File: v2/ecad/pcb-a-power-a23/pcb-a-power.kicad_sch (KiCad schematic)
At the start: 603 parts, among them Q1 2N7002: panel controller high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, Q10 CSD18510Q5B 40 V N-FET, Q11 CSD18510Q5B 40 V N-FET, Q12 CSD18510Q5B 40 V N-FET, Q13 CSD18510Q5B 40 V N-FET, Q14 CSD18510Q5B 40 V N-FET, Q15 CSD18510Q5B 40 V N-FET, Q16 CSD18510Q5B 40 V N-FET, Q17 CSD19532Q5B 100 V N-FET (4.6 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, Q18 CSD19532Q5B 100 V N-FET (4.6 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, Q19 CSD19532Q5B 100 V N-FET (4.6 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, Q2 CSD19532Q5B 100 V N-FET (4.6 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, Q20 CSD19532Q5B 100 V N-FET (4.6 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, Q21 CSD18510Q5B 40 V N-FET, Q22 CSD18510Q5B 40 V N-FET, Q23 CSD18510Q5B 40 V N-FET, Q24 CSD18510Q5B 40 V N-FET, Q25 CSD18510Q5B 40 V N-FET, Q26 CSD18510Q5B 40 V N-FET, Q27 CSD18510Q5B 40 V N-FET (VBUS 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, Q28 CSD19532Q5B 100 V N-FET (4.6 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, Q29 CSD19532Q5B 100 V N-FET (4.6 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, Q3 CSD19532Q5B 100 V N-FET (4.6 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, Q30 CSD19532Q5B 100 V N-FET (4.6 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, Q31 CSD19532Q5B 100 V N-FET (4.6 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, Q32 CSD19532Q5B 100 V N-FET (4.6 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, Q33 CSD19532Q5B 100 V N-FET (4.6 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, Q34 CSD19532Q5B 100 V N-FET (4.6 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, Q35 CSD19532Q5B 100 V N-FET (4.6 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, Q36 2N7002: FE_RUN high = latch s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, Q37 2N7002: FE_RUN high = bleed o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, Q38 CSD19532Q5B 100 V N-FET (the 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, Q4 CSD19532Q5B 100 V N-FET (4.6 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, Q5 CSD19532Q5B 100 V N-FET (4.6 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, Q6 2N7002: CHG_INHIBIT high = IL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, Q7 CSD18510Q5B 40 V N-FET, Q8 CSD18510Q5B 40 V N-FET, Q9 CSD18510Q5B 40 V N-FET, U1 LTC2954ITS8-1 push-button on/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, U10 INA226 rail monitor +5V_S3, U11 INA226 rail monitor +5V_DEV, U12 TPS62933DRLR 3 A buck, 3.3 V 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, U13 LM5176PWPR buck-boost control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, U14 INA226 PA rail monitor (0x46), U15 LM5176PWPR buck-boost control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, U16 LM5176PWPR buck-boost control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, U17 INA226 PoE rail monitor (0x47), U18 TPS25740ARGER USB-C PD source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, U19 LM5176PWPR buck-boost control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, U2 LM5176PWPR buck-boost control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, U21 TPS259631DDAR eFuse VBAT -> V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, U22 TPS259631DDAR eFuse VBAT -> V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, U23 TPS259631DDAR eFuse +5V_DEV -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, U26 SN74LVC08APWR quad AND: the o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, U27 PCA9555PW (0x21): enables and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, U28 PCA9555PW (0x24): power-good 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, U29 USBLC6-2SC6, U3 BQ25731RSNR 1 to 5 cell buck-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, U30 SN74LVC1G00DBVR NAND: OUTLET_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, U31 TPD2E2U06QDBZRQ1 low-capacita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, U32 TPS259631DDAR eFuse +5V_DEV -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, U33 TPS62933DRLR 3 A buck, 12.0 V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, U34 TPS37A010122DSKR 65 V OV/UV s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, U35 SN74AUP1G08DBVR AND: PA_TXOK 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, U36 SN74AUP1G08DBVR AND: PA_EN = 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, U37 SN74AUP1G08DBVR AND: HF_TXOK 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, U38 SN74AUP1G08DBVR AND: HF_EN = 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, U39 TPS259631DDAR eFuse +3V3 -> +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, U4 AP64500SP-13 5 A buck, 5.1 V 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, U40 SN74LVC2G07DBVR dual open-dra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, U5 LM5176PWPR buck-boost control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, U6 AP64500SP-13 5 A buck, 5.1 V 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, U7 LM5176PWPR buck-boost control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, U8 INA226 rail monitor +5V_S1, U9 INA226 rail monitor +5V_S2

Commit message: fix(pcb-d,pcb-e): declare the supplies PWR-001 refused, sense the tracker's current on its bottom leg, and carry VIN_RAW across the dock on power pins with board A's half [MESHSAT-1357]
Boards D and E, stream w3de (27 September 2026, from main 0598e8e5), integrated in fnd/r8int5 on main 68a83858 with
board A's half of EQ-16 on board A's w3a generator. The session's engineering choices are recorded as SC-55 to SC-57
with reason and reversal, never as the owner's. Prototype: no board is built.

PWR-001 (EQ-19): each supply the rule refused on D and E is declared with the kind its maker's sheet gives. The parts'
own regulator outputs, charge pumps and bootstraps are nodes (D: PCM2912A outputs, SAU_3V3, AMP_CPP, AMP_CPN,
AMP_HPVSS; E: TRK_LDO33, E6_DVDD, E6_BST); SGP_VDD, another part's filtered branch, is a rail. PWR-001 read
INCONCLUSIVE on D (RLY_K) and E (FAN1_SW, FAN2_SW) with no failure in the stream's scratch, the three awaiting the
flyback diodes' sheets (S-76).

S-47: the LT8705A's sense resistor R5 moves to the bottom switches' leg as the maker draws it (8705af Figure 1): the
new node TRK_CS joins Q4's and Q5's sources above R5, L1 joins TRK_SW1 to TRK_SW2, MODE is tied to LDO33, GATEVCC and
VIN get their own bypass capacitors (C63, C64). TRK_CS is a switching net in board E's pre-lay group and in
pcb_sensitive.yaml's switch list, as board A's LM5176 CS nodes are.

EQ-16 / R8E-N01: at board E's 14.10 A the four Preci-Dip 813 VIN_RAW contacts ran at 3.53 A each against 3.5 A.
VIN_RAW now crosses the dock on four Mill-Max 9 A power pins with four return pins, as CELL+ does, and the four 813
contacts become ground. Board E's half (J_BLK, P_VR, P_VN) and board A's (J_VR1-4, J_VN1-4, J_DOCK, VIN_RAW declared
at 14.10 A) land together, with the IF-AE-DOCK contract and check_contracts.py's dock checks: PASS 99 of 99 on this
tree's netlists (verdicts in scratch).

Parity: stream w3de regenerated D and E on the KiCad box with main's chain; D's netlist is identical in e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
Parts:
- removed C113, C153, C222, C28, C40: 100n, Capacitor_SMD:C_0603_1608Metric, symbol Device:C
- removed C134, C141, C27: 1n, Capacitor_SMD:C_0603_1608Metric, symbol Device:C
- removed C148, C149: 470p, Capacitor_SMD:C_0603_1608Metric, symbol Device:C
- removed C158, C26: 10n, Capacitor_SMD:C_0603_1608Metric, symbol Device:C
- removed C23, C24: 22u 25V 1210, Capacitor_SMD:C_1210_3225Metric, symbol Device:C
- removed C34, C79: 100n 25V, Capacitor_SMD:C_0603_1608Metric, symbol Device:C
- removed C86, C94: 220n, Capacitor_SMD:C_0603_1608Metric, symbol Device:C
- removed C87: 1.5n, Capacitor_SMD:C_0603_1608Metric, symbol Device:C
- removed C88: 47n, Capacitor_SMD:C_0603_1608Metric, symbol Device:C
- removed D15, D16: BAT46W-7-F Schottky 100V (bootstrap), Diode_SMD:D_SOD-123, symbol Device:D_Schottky
- removed D22: BZT52C12-7-F zener, the restart guard's pull-up c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, Diode_SMD:D_SOD-123, symbol Device:D_Zener
- removed J_BM11: SMP-MAX slide-on receptacle R222M00720 (underside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, meshsat:Radiall_SMPMAX_R222M00720, symbol Connector:Conn_Coaxial
- removed L10: 15uH XAL1010-153ME (Isat 15.5 A), Inductor_SMD:L_Coilcraft_XAL1010-XXX, symbol Device:L
- removed Q19: CSD19532Q5B 100 V N-FET (4.6 mOhm at VGS 6 V, Pow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, Package_SO:PowerPAK_SO-8_Single, symbol meshsat_ic:Q19
- removed R10: 15k, Resistor_SMD:R_0603_1608Metric, symbol Device:R
- removed R123, R178, R30: 100k, Resistor_SMD:R_0603_1608Metric, symbol Device:R
- removed R130: 2.2k, Resistor_SMD:R_0603_1608Metric, symbol Device:R
- removed R137: 14.0k 1% (R_FBL1: 15 V when CTL1 is low too), Resistor_SMD:R_0603_1608Metric, symbol Device:R
- removed R15, R51: 10k 1%, Resistor_SMD:R_0603_1608Metric, symbol Device:R
- removed R180: 100R 1% (CS filter, Kelvin from the shunt's top), Resistor_SMD:R_0603_1608Metric, symbol Device:R
- removed R23, R25: 10k, Resistor_SMD:R_0603_1608Metric, symbol Device:R
- removed R27: 40.2k 1%, Resistor_SMD:R_0603_1608Metric, symbol Device:R
- removed R32, R40: 53.6k 1%, Resistor_SMD:R_0603_1608Metric, symbol Device:R
- removed R80: 3.3k, Resistor_SMD:R_0603_1608Metric, symbol Device:R
- removed U22: TPS259631DDAR eFuse VBAT -> VHEAT_IN (909R 1% (IL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, Package_SO:SOIC-8-1EP_3.9x4.9mm_P1.27mm_EP2.29x3mm, symbol meshsat_ic:U22
- added C112: 3.3n, Capacitor_SMD:C_0603_1608Metric, symbol Device:C
- added C119, C21, C22, C74, C82: 10u 50V X7R 1210, Capacitor_SMD:C_1210_3225Metric, symbol Device:C
- added C138: 1n, Capacitor_SMD:C_0603_1608Metric, symbol Device:C
- added C144, C16, C46, C90: 100n 25V, Capacitor_SMD:C_0603_1608Metric, symbol Device:C
- added C161, C37: 22u 25V 1210, Capacitor_SMD:C_1210_3225Metric, symbol Device:C
- added C174: 470u 25V Panasonic EEHZK1E471P hybrid polymer (10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, Capacitor_SMD:CP_Elec_10x10, symbol Device:C_Polarized
- added C18: 3.3u, Capacitor_SMD:C_0805_2012Metric, symbol Device:C
- added C193, C197, C219, C221: 100n, Capacitor_SMD:C_0603_1608Metric, symbol Device:C
- added C41: 10u 25V 1210, Capacitor_SMD:C_1210_3225Metric, symbol Device:C
- added C60: 4.7u, Capacitor_SMD:C_0805_2012Metric, symbol Device:C
- added C83: 10u 100V X7R 1210, Capacitor_SMD:C_1210_3225Metric, symbol Device:C
- added D12, D14, D17, D18, D8: BAT46W-7-F Schottky 100V (bootstrap), Diode_SMD:D_SOD-123, symbol Device:D_Schottky
- added J_VN1, J_VN2, J_VN3, J_VN4: 9 A spring pin, VIN_RAW return (Mill-Max 0858 cla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, meshsat:Mill-Max_0858_power_pin, symbol Connector:Conn_01x01_Pin
- added J_VR1, J_VR2, J_VR3, J_VR4: 9 A spring pin, VIN_RAW (Mill-Max 0858 class, doc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, meshsat:Mill-Max_0858_power_pin, symbol Connector:Conn_01x01_Pin
- added L1: 10uH XAL1010-103ME (Isat 17.5 A), Inductor_SMD:L_Coilcraft_XAL1010-XXX, symbol Device:L
- added L2: 3.3uH XAL6030-332ME (Isat 12.2 A), Inductor_SMD:L_Coilcraft_XAL6060-XXX, symbol Device:L
- added L3: 4.7uH XAL6060-472ME (Isat 11 A), Inductor_SMD:L_Coilcraft_XAL6060-XXX, symbol Device:L
- added L6: 6.8uH XAL1010-682ME (Isat 21.8 A), Inductor_SMD:L_Coilcraft_XAL1010-XXX, symbol Device:L
- added Q22: CSD18510Q5B 40 V N-FET, Package_SO:PowerPAK_SO-8_Single, symbol meshsat_ic:Q22
- added Q36: 2N7002: FE_RUN high = latch sense held at 0 V (1 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, Package_TO_SOT_SMD:SOT-23, symbol Transistor_FET:2N7002
- added Q38: CSD19532Q5B 100 V N-FET (the VBUS20 bleed switch), Package_SO:PowerPAK_SO-8_Single, symbol meshsat_ic:Q38
- added R139: 43R 1W 2512 (DSCG), Resistor_SMD:R_2512_6332Metric, symbol Device:R
- added R171: 100k, Resistor_SMD:R_0603_1608Metric, symbol Device:R
- added R18: 10R, Resistor_SMD:R_0603_1608Metric, symbol Device:R
- added R19: 16.5k 1%, Resistor_SMD:R_0603_1608Metric, symbol Device:R
- added R96: 143k 1%, Resistor_SMD:R_0603_1608Metric, symbol Device:R
- added TP17: SDA, TestPoint:TestPoint_Pad_D1.5mm, symbol Connector:TestPoint
- added U17: INA226 PoE rail monitor (0x47), Package_SO:VSSOP-10_3x3mm_P0.5mm, symbol meshsat_ic:U17
- added U27: PCA9555PW (0x21): enables and status, Package_SO:TSSOP-24_4.4x7.8mm_P0.65mm, symbol Interface_Expansion:PCA9555PW
- C113: renamed from R171; value 100k -> 100n; footprint Resistor_SMD:R_0603_1608Metric -> Capacitor_SMD:C_0603_1608Metric; symbol Device:R -> Device:C; LCSC (none) -> C14663
- C117: renamed from C90; value 100n 25V -> 10u 50V X7R 1210; footprint Capacitor_SMD:C_0603_1608Metric -> Capacitor_SMD:C_1210_3225Metric
- C118: renamed from D17; value BAT46W-7-F Schottky 100V (bootstrap) -> 10u 50V X7R 1210; footprint Diode_SMD:D_SOD-123 -> Capacitor_SMD:C_1210_3225Metric; symbol Device:D_Schottky -> Device:C; LCSC C83152 -> (none)
- C134: renamed from C137; value 100n 25V -> 1n; LCSC (none) -> C1588
- C137: renamed from C193; value 100n -> 100n 25V
- C141: renamed from C146; LCSC (none) -> C1588
- C146: renamed from C144; value 100n 25V -> 1n
- C148: renamed from D12; value BAT46W-7-F Schottky 100V (bootstrap) -> 470p; footprint Diode_SMD:D_SOD-123 -> Capacitor_SMD:C_0603_1608Metric; symbol Device:D_Schottky -> Device:C; LCSC C83152 -> C27694
- C149: renamed from D14; value BAT46W-7-F Schottky 100V (bootstrap) -> 470p; footprint Diode_SMD:D_SOD-123 -> Capacitor_SMD:C_0603_1608Metric; symbol Device:D_Schottky -> Device:C; LCSC C83152 -> C27694
- C153: renamed from U27; value PCA9555PW (0x21): enables and status -> 100n; footprint Package_SO:TSSOP-24_4.4x7.8mm_P0.65mm -> Capacitor_SMD:C_0603_1608Metric; symbol Interface_Expansion:PCA9555PW -> Device:C; LCSC C2864778 -> (none)
- C158: renamed from C161; value 22u 25V 1210 -> 10n; footprint Capacitor_SMD:C_1210_3225Metric -> Capacitor_SMD:C_0603_1608Metric
- C17: renamed from L2; value 3.3uH XAL6030-332ME (Isat 12.2 A) -> 100n 25V; footprint Inductor_SMD:L_Coilcraft_XAL6060-XXX -> Capacitor_SMD:C_0603_1608Metric; symbol Device:L -> Device:C
- C222: renamed from Q22; value CSD18510Q5B 40 V N-FET -> 100n; footprint Package_SO:PowerPAK_SO-8_Single -> Capacitor_SMD:C_0603_1608Metric; symbol meshsat_ic:Q22 -> Device:C; LCSC (none) -> C14663
- C23: renamed from C21; value 10u 50V X7R 1210 -> 22u 25V 1210
- C24: renamed from C22; value 10u 50V X7R 1210 -> 22u 25V 1210
- C26: renamed from R18; value 10R -> 10n; footprint Resistor_SMD:R_0603_1608Metric -> Capacitor_SMD:C_0603_1608Metric; symbol Device:R -> Device:C
- C27: renamed from R19; value 16.5k 1% -> 1n; footprint Resistor_SMD:R_0603_1608Metric -> Capacitor_SMD:C_0603_1608Metric; symbol Device:R -> Device:C
- C28: renamed from C112; value 3.3n -> 100n
- C34: renamed from C37; value 22u 25V 1210 -> 100n 25V; footprint Capacitor_SMD:C_1210_3225Metric -> Capacitor_SMD:C_0603_1608Metric; LCSC C2918511 -> (none)
- C40: renamed from C41; value 10u 25V 1210 -> 100n; footprint Capacitor_SMD:C_1210_3225Metric -> Capacitor_SMD:C_0603_1608Metric
- C79: renamed from C197; value 100n -> 100n 25V
- C86: renamed from C119; value 10u 50V X7R 1210 -> 220n; footprint Capacitor_SMD:C_1210_3225Metric -> Capacitor_SMD:C_0603_1608Metric; LCSC (none) -> C160828
- C87: renamed from C174; value 470u 25V Panasonic EEHZK1E471P hybrid polymer (10.2 mm) -> 1.5n; footprint Capacitor_SMD:CP_Elec_10x10 -> Capacitor_SMD:C_0603_1608Metric; symbol Device:C_Polarized -> Device:C; LCSC C242138 -> C37788
- C88: renamed from C117; value 10u 50V X7R 1210 -> 47n; footprint Capacitor_SMD:C_1210_3225Metric -> Capacitor_SMD:C_0603_1608Metric
- C94: renamed from R139; value 43R 1W 2512 (DSCG) -> 220n; footprint Resistor_SMD:R_2512_6332Metric -> Capacitor_SMD:C_0603_1608Metric; symbol Device:R -> Device:C
- D15: renamed from C221; value 100n -> BAT46W-7-F Schottky 100V (bootstrap); footprint Capacitor_SMD:C_0603_1608Metric -> Diode_SMD:D_SOD-123; symbol Device:C -> Device:D_Schottky; LCSC C14663 -> C83152
- D16: renamed from C82; value 10u 50V X7R 1210 -> BAT46W-7-F Schottky 100V (bootstrap); footprint Capacitor_SMD:C_1210_3225Metric -> Diode_SMD:D_SOD-123; symbol Device:C -> Device:D_Schottky; LCSC (none) -> C83152
- D22: renamed from Q38; value CSD19532Q5B 100 V N-FET (the VBUS20 bleed switch) -> BZT52C12-7-F zener, the restart guard's pull-up clamp; footprint Package_SO:PowerPAK_SO-8_Single -> Diode_SMD:D_SOD-123; symbol meshsat_ic:Q38 -> Device:D_Zener; LCSC C473333 -> C124196
- D6: renamed from C219; value 100n -> BAT46W-7-F Schottky 100V (bootstrap); footprint Capacitor_SMD:C_0603_1608Metric -> Diode_SMD:D_SOD-123; symbol Device:C -> Device:D_Schottky; LCSC C14663 -> C83152
- J_BM11: renamed from TP17; value SDA -> SMP-MAX slide-on receptacle R222M00720 (underside), LORA to the dock plug; footprint TestPoint:TestPoint_Pad_D1.5mm -> meshsat:Radiall_SMPMAX_R222M00720; symbol Connector:TestPoint -> Connector:Conn_Coaxial; now in the parts list
- J_DOCK: value spring pins to the dock block (2x6, Preci-Dip 813-S1-012-10-016101, underside): 1-4 VIN_RAW (9 to 36 V from E6), 5-7 GN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 -> spring pins to the dock block (2x6, Preci-Dip 813-S1-012-10-016101, underside): 1-7 GND, 8 SHORE_INHIBIT, 9-10 USB of E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
- L10: renamed from C83; value 10u 100V X7R 1210 -> 15uH XAL1010-153ME (Isat 15.5 A); footprint Capacitor_SMD:C_1210_3225Metric -> Inductor_SMD:L_Coilcraft_XAL1010-XXX; symbol Device:C -> Device:L; LCSC (none) -> C2802562
- Q19: renamed from U17; value INA226 PoE rail monitor (0x47) -> CSD19532Q5B 100 V N-FET (4.6 mOhm at VGS 6 V, PowerPAK SO-8 / SON-8 5x6); footprint Package_SO:VSSOP-10_3x3mm_P0.5mm -> Package_SO:PowerPAK_SO-8_Single; symbol meshsat_ic:U17 -> meshsat_ic:Q19; LCSC C49851 -> C473333
- R10: renamed from L1; value 10uH XAL1010-103ME (Isat 17.5 A) -> 15k; footprint Inductor_SMD:L_Coilcraft_XAL1010-XXX -> Resistor_SMD:R_0603_1608Metric; symbol Device:L -> Device:R; LCSC C6358489 -> C22809
- R123: renamed from C74; value 10u 50V X7R 1210 -> 100k; footprint Capacitor_SMD:C_1210_3225Metric -> Resistor_SMD:R_0603_1608Metric; symbol Device:C -> Device:R
- R130: renamed from C138; value 1n -> 2.2k; footprint Capacitor_SMD:C_0603_1608Metric -> Resistor_SMD:R_0603_1608Metric; symbol Device:C -> Device:R; LCSC (none) -> C4190
- R137: renamed from D18; value BAT46W-7-F Schottky 100V (bootstrap) -> 14.0k 1% (R_FBL1: 15 V when CTL1 is low too); footprint Diode_SMD:D_SOD-123 -> Resistor_SMD:R_0603_1608Metric; symbol Device:D_Schottky -> Device:R; LCSC C83152 -> (none)
- R15: renamed from Q36; value 2N7002: FE_RUN high = latch sense held at 0 V (1 G, 2 S, 3 D) -> 10k 1%; footprint Package_TO_SOT_SMD:SOT-23 -> Resistor_SMD:R_0603_1608Metric; symbol Transistor_FET:2N7002 -> Device:R; LCSC C8545 -> C25804
- R178: renamed from L6; value 6.8uH XAL1010-682ME (Isat 21.8 A) -> 100k; footprint Inductor_SMD:L_Coilcraft_XAL1010-XXX -> Resistor_SMD:R_0603_1608Metric; symbol Device:L -> Device:R
- R180: renamed from C46; value 100n 25V -> 100R 1% (CS filter, Kelvin from the shunt's top); footprint Capacitor_SMD:C_0603_1608Metric -> Resistor_SMD:R_0603_1608Metric; symbol Device:C -> Device:R
- R181: renamed from D8; value BAT46W-7-F Schottky 100V (bootstrap) -> 100R 1% (CSG filter, Kelvin from the shunt's ground pad); footprint Diode_SMD:D_SOD-123 -> Resistor_SMD:R_0603_1608Metric; symbol Device:D_Schottky -> Device:R; LCSC C83152 -> (none)
- R23: renamed from C17; value 100n 25V -> 10k; footprint Capacitor_SMD:C_0603_1608Metric -> Resistor_SMD:R_0603_1608Metric; symbol Device:C -> Device:R
- R25: renamed from C18; value 3.3u -> 10k; footprint Capacitor_SMD:C_0805_2012Metric -> Resistor_SMD:R_0603_1608Metric; symbol Device:C -> Device:R
- R27: renamed from C16; value 100n 25V -> 40.2k 1%; footprint Capacitor_SMD:C_0603_1608Metric -> Resistor_SMD:R_0603_1608Metric; symbol Device:C -> Device:R
- R30: renamed from L3; value 4.7uH XAL6060-472ME (Isat 11 A) -> 100k; footprint Inductor_SMD:L_Coilcraft_XAL6060-XXX -> Resistor_SMD:R_0603_1608Metric; symbol Device:L -> Device:R
- R32: renamed from D6; value BAT46W-7-F Schottky 100V (bootstrap) -> 53.6k 1%; footprint Diode_SMD:D_SOD-123 -> Resistor_SMD:R_0603_1608Metric; symbol Device:D_Schottky -> Device:R; LCSC C83152 -> (none)
- R40: renamed from R181; value 100R 1% (CSG filter, Kelvin from the shunt's ground pad) -> 53.6k 1%
- R51: renamed from C60; value 4.7u -> 10k 1%; footprint Capacitor_SMD:C_0805_2012Metric -> Resistor_SMD:R_0603_1608Metric; symbol Device:C -> Device:R
- R80: renamed from C118; value 10u 50V X7R 1210 -> 3.3k; footprint Capacitor_SMD:C_1210_3225Metric -> Resistor_SMD:R_0603_1608Metric; symbol Device:C -> Device:R; LCSC (none) -> C22978
- U22: renamed from R96; value 143k 1% -> TPS259631DDAR eFuse VBAT -> VHEAT_IN (909R 1% (ILM: 1.0 A)); footprint Resistor_SMD:R_0603_1608Metric -> Package_SO:SOIC-8-1EP_3.9x4.9mm_P1.27mm_EP2.29x3mm; symbol Device:R -> meshsat_ic:U22; LCSC C22877 -> C2155778
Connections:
- net +3V3: now also C153.1, R123.2, R178.2, R23.2, R171.2, U17.1 (+3V3), U17.6 (+3V3), U27.21 (A0), U27.24 (VDD); no longer C113.2, C153.21 (A0), C153.24 (VDD), Q19.1 (+3V3), Q19.6 (+3V3)
- net +54V_POE: now also C83.1, U17.9 (+54V_POE); no longer L10.1, Q19.9 (+54V_POE)
- net +5V_DEV: now also R40.1
- net +5V_S2: now also R32.1, C37.1; no longer C34.1
- net CHG_ILIM: now also R19.2; no longer C27.2
- net CHG_INHIBIT: now also U27.4 (IO0_0); no longer C153.4 (IO0_0)
- net CHRG_OK: now also U27.13 (IO1_0); no longer C153.13 (IO1_0)
- net CH_BTST1: now also C16.1; no longer R27.1
- net CH_BTST2: now also C17.1; no longer R23.1
- net CH_CELL: now also R27.1
- net CH_COMP1: now also R25.1
- net CH_COMP1C: now also C26.1, R25.2
- net CH_COMP2: now also C27.1
- net CH_SW1: now also C16.2, L2.1; no longer C17.1, R27.2
- net CH_SW2: now also L2.2; no longer R23.2
- net CH_VDDA: now also R18.2; no longer C26.2
- net D8_EN: now also U27.7 (IO0_3); no longer C153.7 (IO0_3)
- net D8_FLT: now also U27.17 (IO1_4); no longer C153.17 (IO1_4)
- net DEV_EN: now also U27.11 (IO0_7); no longer C153.11 (IO0_7)
- net DOCK_SPARE: now also U27.18 (IO1_5); no longer C153.18 (IO1_5)
- net EXP_INT: now also U27.1 (~{INT}); no longer C153.1 (~{INT})
- net FE_BLEED: now also Q38.5 (FE_BLEED); no longer D22.5 (FE_BLEED)
- net FE_BLEED_G: now also Q38.4 (FE_BLEED_G); no longer D22.4 (FE_BLEED_G)
- net FE_COMP: now also R10.1
- net FE_COMPC: now also R10.2
- net FE_LATCH: now also Q36.3 (D); no longer R15.3 (D)
- net FE_PGOOD: now also U27.20 (IO1_7); no longer C153.20 (IO1_7)
- net FE_RUN: now also Q36.1 (G); no longer R15.1 (G)
- net FE_SW1: now also L1.1; no longer R10.1
- net FE_SW2: now also L1.2; no longer R10.2
- net FE_UVS: now also R15.1
- net FE_VZ: now also D22.1 (K)
- net GND: now also C113.2, C117.2, C118.2, C134.2, C141.2, C148.2, C149.2, C222.2, C26.2, C27.2, C94.2, J_BM11.2 (Ext)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; no longer C137.2, C153.12 (VSS), C153.3 (A2), C28.2, C34.2, C40.2, C79.2, D15.2, D16.2, D22.1 (GND), D22.3 (GND), D6.2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
- net HEAT_EN: now also U22.3 (HEAT_EN), U27.6 (IO0_2); no longer C153.6 (IO0_2)
- net HEAT_FLT: now also U22.6 (HEAT_FLT), U27.16 (IO1_3); no longer C153.16 (IO1_3)
- net HF_BOOT2: now also D14.1 (K); no longer C149.1 (K)
- net HF_PGOOD: now also R123.1
- net HF_SLOPE: now also C149.1
- net HF_SW_EN: now also U27.10 (IO0_6); no longer C153.10 (IO0_6)
- net HF_VCC: now also D14.2 (A); no longer C149.2 (A)
- net HT_SS: now also C158.1
- net INA_ALERT: now also U17.3 (INA_ALERT), U27.19 (IO1_6); no longer C153.19 (IO1_6), Q19.3 (INA_ALERT)
- net MON_EN: now also U27.5 (IO0_1); no longer C153.5 (IO0_1)
- net MON_FLT: now also U27.15 (IO1_2); no longer C153.15 (IO1_2)
- net PA_BOOT2: now also D12.1 (K); no longer C148.1 (K)
- net PA_FB: now also R51.1
- net PA_SLOPE: now also C148.1
- net PA_SW_EN: now also U27.9 (IO0_5); no longer C153.9 (IO0_5)
- net PA_VCC: now also C60.1, D12.2 (A); no longer C148.2 (A), R51.1
- net PD_BOOT1: now also C90.1, D17.1 (K); no longer C117.1, C118.1 (K)
- net PD_BOOT2: now also D18.1 (K); no longer R137.1 (K)
- net PD_COMP: now also C87.1, R80.1
- net PD_COMPC: now also C86.1, R80.2
- net PD_CS: now also Q22.1 (PD_CS), Q22.2 (PD_CS), Q22.3 (PD_CS); no longer C222.1 (PD_CS), C222.2 (PD_CS), C222.3 (PD_CS)
- net PD_CTL1: now also R137.2
- net PD_DSCG: now also R139.1; no longer C94.1
- net PD_DVDD: now also C94.1
- net PD_FB: now also R137.1
- net PD_LDRV1: now also Q22.4 (PD_LDRV1); no longer C222.4 (PD_LDRV1)
- net PD_SS: now also C88.1
- net PD_SW1: now also C90.2, Q22.5 (PD_SW1); no longer C117.2, C222.5 (PD_SW1)
- net PD_VBUS: now also R139.2; no longer C94.2
- net PD_VCC: now also D17.2 (A), D18.2 (A); no longer C118.2 (A), R137.2 (A)
- net PD_VPWR: now also C117.1, C118.1, C119.1, C174.1; no longer C86.1, C87.1, C88.1, R80.1
- net POE_BOOT1: now also C79.1, D15.1 (K)
- net POE_BOOT2: now also D16.1 (K)
- net POE_CS: now also Q19.1 (POE_CS), Q19.2 (POE_CS), Q19.3 (POE_CS)
- net POE_LDRV2: now also Q19.4 (POE_LDRV2)
- net POE_OUT: now also U17.10 (POE_OUT); no longer Q19.10 (POE_OUT)
- net POE_SW1: now also C79.2, L10.1
- net POE_SW2: now also L10.2, Q19.5 (POE_SW2)
- net POE_SW_EN: now also U27.8 (IO0_4); no longer C153.8 (IO0_4)
- net POE_VCC: now also D15.2 (A), D16.2 (A)
- net PROCHOT: now also R23.1, U27.14 (IO1_1); no longer C153.14 (IO1_1)
- net REGN: now also C18.1, R18.1, R19.1; no longer C26.1, C27.1, R25.1
- net RF_LORA: now also J_BM11.1 (In)
- net S1_BOOT: now also C28.1
- net S1_COMPC: now also C112.1; no longer C28.1
- net S1_OUT: now also L3.2; no longer R30.2
- net S1_SW: now also C28.2, L3.1; no longer R30.1
- net S2_BOOT1: now also C34.1
- net S2_BOOT2: now also C137.1, D6.1 (K); no longer C134.1, R32.1 (K)
- net S2_COMP: now also C134.1, R130.1
- net S2_COMPC: now also C113.1, R130.2
- net S2_CSF: now also C138.1; no longer R130.1
- net S2_CSGF: now also C138.2; no longer R130.2
- net S2_FB: now also R32.2
- net S2_PGOOD: now also R171.1; no longer C113.1
- net S2_SW1: now also C34.2
- net S2_SW2: now also C137.2; no longer C134.2
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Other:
- note added: "CHARGER BQ25731 | SLOT RAIL S1"
- note added: "CHARGER BQ25731: 4S FROM THE 20 V BUS, SYSTEM ON VSYS (VBAT), PACK BEYOND RSR, I2C 0x6B (continued)"
- note added: "DEVICE RAIL | 3.3 V LOGIC"
- note added: "DEVICE RAIL: LM5176 5.1 V (7.2 A MINIMUM LIMIT) + INA226 0x45 (continued)"
- note added: "HF RAIL"
- note added: "PA RAIL"
- note added: "PACK NODE OVER THE DOCK BLOCK (32.56) | MAIN POWER CONTROL LTC2954"
- note added: "SLOT RAIL S2"
- note added: "SLOT RAIL S3 | DEVICE RAIL"
- note added: "p1,15"
- note added: "p1,7,13"
- note added: "p1,7,15"
- note added: "p10,16"
- note added: "p11,12,16"
- note added: "p11,15"
- note added: "p11,15,16"
- note added: "p11,16"
- note added: "p12,15,16"
- note added: "p13,15"
- note added: "p15,16"
- note added: "p16"
- note added: "p2,16"
- note added: "p3,4,5,7,.."
- note added: "p3,4,6,7,.."
- note added: "p3,5,6,7,.."
- note added: "p4,15"
- note added: "p4,16"
- note added: "p4,5,6,7,.."
- note added: "p4,5,7,8,.."
- note added: "p5,6,7,8,.."
- note added: "p7,13,15"
- note added: "p8,13"
- note added: "p8,16"
- note added: "p9,16"
- note added: "page 1 of 16 MeshSat field kit V2, CERN-OHL-S-2.0 PROTOTYPE, nothing built 2026-09-27"
- note added: "page 10 of 16 MeshSat field kit V2, CERN-OHL-S-2.0 PROTOTYPE, nothing built 2026-09-27"
- note added: "page 11 of 16 MeshSat field kit V2, CERN-OHL-S-2.0 PROTOTYPE, nothing built 2026-09-27"
- note added: "page 12 of 16 MeshSat field kit V2, CERN-OHL-S-2.0 PROTOTYPE, nothing built 2026-09-27"
- note added: "page 13 of 16 MeshSat field kit V2, CERN-OHL-S-2.0 PROTOTYPE, nothing built 2026-09-27"
- note added: "page 14 of 16 MeshSat field kit V2, CERN-OHL-S-2.0 PROTOTYPE, nothing built 2026-09-27"
- note added: "page 15 of 16 MeshSat field kit V2, CERN-OHL-S-2.0 PROTOTYPE, nothing built 2026-09-27"
- note added: "page 16 of 16 MeshSat field kit V2, CERN-OHL-S-2.0 PROTOTYPE, nothing built 2026-09-27"
- note added: "page 2 of 16 MeshSat field kit V2, CERN-OHL-S-2.0 PROTOTYPE, nothing built 2026-09-27"
- note added: "page 3 of 16 MeshSat field kit V2, CERN-OHL-S-2.0 PROTOTYPE, nothing built 2026-09-27"
- note added: "page 4 of 16 MeshSat field kit V2, CERN-OHL-S-2.0 PROTOTYPE, nothing built 2026-09-27"
- note added: "page 5 of 16 MeshSat field kit V2, CERN-OHL-S-2.0 PROTOTYPE, nothing built 2026-09-27"
- note added: "page 6 of 16 MeshSat field kit V2, CERN-OHL-S-2.0 PROTOTYPE, nothing built 2026-09-27"
- note added: "page 7 of 16 MeshSat field kit V2, CERN-OHL-S-2.0 PROTOTYPE, nothing built 2026-09-27"
- note added: "page 8 of 16 MeshSat field kit V2, CERN-OHL-S-2.0 PROTOTYPE, nothing built 2026-09-27"
- note added: "page 9 of 16 MeshSat field kit V2, CERN-OHL-S-2.0 PROTOTYPE, nothing built 2026-09-27"
- note removed: "3.3 V LOGIC | PA RAIL"
- note removed: "DEVICE RAIL"
- note removed: "PA RAIL | HF RAIL"
- note removed: "PA RAIL: LM5176 13.8 V 6 A, EMCON GATED, INA226 0x46 (continued)"
- note removed: "PACK NODE OVER THE DOCK BLOCK (32.56) | MAIN POWER CONTROL LTC2954 | FRONT END"
- note removed: "SLOT RAIL S1 | SLOT RAIL S2"
- note removed: "SLOT RAIL S2 | SLOT RAIL S3"
- note removed: "SLOT RAIL S2: LM5176 5.1 V (7.2 A MINIMUM LIMIT) + INA226 0x41 (continued)"
- note removed: "p1,13"
- note removed: "p1,7,12"
- note removed: "p1,7,14"
- note removed: "p10,11,15"
- note removed: "p10,14"
- note removed: "p10,14,15"
- note removed: "p11,12"
- note removed: "p11,13"
- note removed: "p11,14,15"
- note removed: "p2,14"
- note removed: "p3,14"
- note removed: "p3,15"
- note removed: "p3,4,5,8,.."
- note removed: "p3,4,6,8,.."
- note removed: "p3,5,6,8,.."
- note removed: "p4,5,6,8,.."
- note removed: "p4,6,8,9,.."
- note removed: "p5,6,8,9,.."
- note removed: "p7,12"
- note removed: "p7,12,14"
- note removed: "p7,13"
- note removed: "p7,14,15"
- note removed: "p7,8,14"
- note removed: "p7,8,15"
- note removed: "p8,14,15"
- note removed: "p9,14"
- note removed: "page 1 of 15 MeshSat field kit V2, CERN-OHL-S-2.0 PROTOTYPE, nothing built 2026-09-27"
- note removed: "page 10 of 15 MeshSat field kit V2, CERN-OHL-S-2.0 PROTOTYPE, nothing built 2026-09-27"
- note removed: "page 11 of 15 MeshSat field kit V2, CERN-OHL-S-2.0 PROTOTYPE, nothing built 2026-09-27"
- note removed: "page 12 of 15 MeshSat field kit V2, CERN-OHL-S-2.0 PROTOTYPE, nothing built 2026-09-27"
- note removed: "page 13 of 15 MeshSat field kit V2, CERN-OHL-S-2.0 PROTOTYPE, nothing built 2026-09-27"
- note removed: "page 14 of 15 MeshSat field kit V2, CERN-OHL-S-2.0 PROTOTYPE, nothing built 2026-09-27"
- note removed: "page 15 of 15 MeshSat field kit V2, CERN-OHL-S-2.0 PROTOTYPE, nothing built 2026-09-27"
- note removed: "page 2 of 15 MeshSat field kit V2, CERN-OHL-S-2.0 PROTOTYPE, nothing built 2026-09-27"
- note removed: "page 3 of 15 MeshSat field kit V2, CERN-OHL-S-2.0 PROTOTYPE, nothing built 2026-09-27"
- note removed: "page 4 of 15 MeshSat field kit V2, CERN-OHL-S-2.0 PROTOTYPE, nothing built 2026-09-27"
- note removed: "page 5 of 15 MeshSat field kit V2, CERN-OHL-S-2.0 PROTOTYPE, nothing built 2026-09-27"
- note removed: "page 6 of 15 MeshSat field kit V2, CERN-OHL-S-2.0 PROTOTYPE, nothing built 2026-09-27"
- note removed: "page 7 of 15 MeshSat field kit V2, CERN-OHL-S-2.0 PROTOTYPE, nothing built 2026-09-27"
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
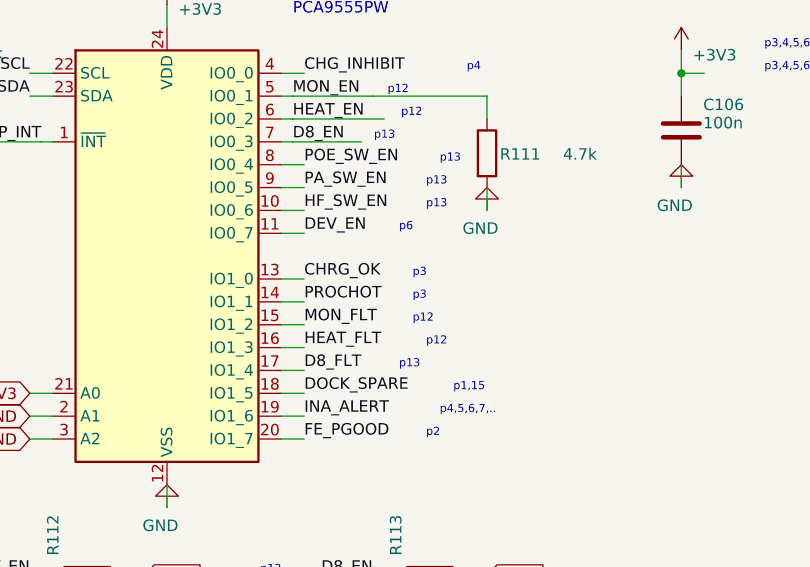
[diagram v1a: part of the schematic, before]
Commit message: feat(boards-a-e): the hot stop line HOT-R1 drawn on boards A and E, and board E's fan flyback sheet filed so PWR-001 reads PASS there [MESHSAT-1357]
Stream w4ae, from main 91894cd7, integrated with its drafts by r8int6 on main 6ec37197 after the w4r, w4b and w4c commits. Prototype design: nothing is built, ordered or measured.

HOT-R1 (S-57, SC-50, REQ-077). Board E: the sensor controller's GPIO19 (U10 pin 30) drives HOT_R1_G, the gate of Q11 (2N7002, the C8545 part of Q8 to Q10). Q11's open drain pulls BLK_SPARE (J_BLK pin 12, TP7) low, and R58 (100 k) holds the gate off while the controller is unpowered, in reset or booting. Board A: R216 (10 k 0603, as R110) pulls DOCK_SPARE (J_DOCK pin 12, U27 pin 18 P1.5, TP21) up to +3V3. No new part number and no new contact. The line is declared a safety line on both boards (A listens, safe high; E is the source), and the net names are kept.

The H2 path, read hop by hop on the committed netlists by v2/docs/records/w4ae/hot_r1_trace.py (on main's netlists it stops at U10 pin 30): an edge on U27 P1.5 raises EXP_INT (J_AB1 pin 13, board B, J_PANEL pin 6) at the panel controller's GPIO24. The panel controller reads U27 on the kit bus and, on a held low, drives PI_KILL (GPIO19, J_PANEL pin 25, board B, J_AB1 pin 10) into Q1. Q1 takes the LTC2954's KILL low, which drops RAIL_EN. No compute-module part is on the path: U27 runs on board A's +3V3, the panel controller on +5V_DEV, the sensor controller on CELL_F. The path is firmware in two controllers; S-58 stays open.

Board E's half of S-76 (SC-65). D7 and D8 carry their order code C51897884 (JLCPCB: SS14, Zhengxin, SMB). The maker's sheet is filed at v2/vendor/zhengxin/zhengxin-ss12-ss120-c51897884.pdf. FAN1_SW and FAN2_SW are declared nodes at 17.35 V (CELL_F's 16.8 V plus 0.55 V at 2.0 A).

Regenerated on the KiCad box with main's chain (PHASE A65 and E42P). Main's generators reproduce main's files and the new generators reproduce their own. The independent netlist comparison f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
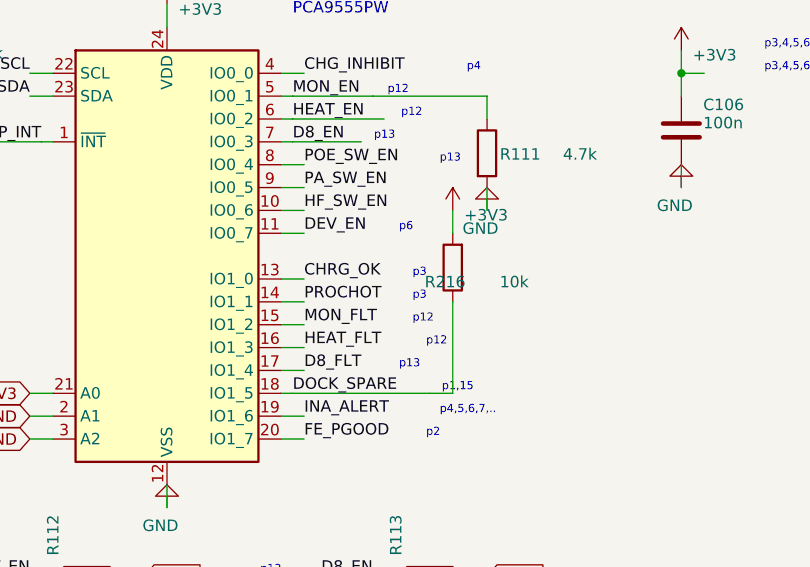
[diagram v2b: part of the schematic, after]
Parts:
- removed C123, C124, C125, C126, C127, C128, C129, C130, C131: 1n, Capacitor_SMD:C_0603_1608Metric, symbol Device:C
- added R152, R154, R156, R158: 100R 1% (CS filter, Kelvin from the shunt's top), Resistor_SMD:R_0603_1608Metric, symbol Device:R
- added R160, R162, R164, R166, R168: 100R 1% (ISNS+ filter, Kelvin from the shunt's ou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, Resistor_SMD:R_0603_1608Metric, symbol Device:R
- added R216: 10k, Resistor_SMD:R_0603_1608Metric, symbol Device:R
- C121: renamed from R148; value 10R -> 10n; footprint Resistor_SMD:R_0603_1608Metric -> Capacitor_SMD:C_0603_1608Metric; symbol Device:R -> Device:C
- C122: renamed from R152; value 100R 1% (CS filter, Kelvin from the shunt's top) -> 100n; footprint Resistor_SMD:R_0603_1608Metric -> Capacitor_SMD:C_0603_1608Metric; symbol Device:R -> Device:C
- C123: renamed from R160; value 100R 1% (ISNS+ filter, Kelvin from the shunt's output pad) -> 1n; footprint Resistor_SMD:R_0603_1608Metric -> Capacitor_SMD:C_0603_1608Metric; symbol Device:R -> Device:C
- C124: renamed from R162; value 100R 1% (ISNS+ filter, Kelvin from the shunt's output pad) -> 1n; footprint Resistor_SMD:R_0603_1608Metric -> Capacitor_SMD:C_0603_1608Metric; symbol Device:R -> Device:C
- C125: renamed from R164; value 100R 1% (ISNS+ filter, Kelvin from the shunt's output pad) -> 1n; footprint Resistor_SMD:R_0603_1608Metric -> Capacitor_SMD:C_0603_1608Metric; symbol Device:R -> Device:C
- C126: renamed from R166; value 100R 1% (ISNS+ filter, Kelvin from the shunt's output pad) -> 1n; footprint Resistor_SMD:R_0603_1608Metric -> Capacitor_SMD:C_0603_1608Metric; symbol Device:R -> Device:C
- C127: renamed from R168; value 100R 1% (ISNS+ filter, Kelvin from the shunt's output pad) -> 1n; footprint Resistor_SMD:R_0603_1608Metric -> Capacitor_SMD:C_0603_1608Metric; symbol Device:R -> Device:C
- C128: renamed from R146; value 10R -> 1n; footprint Resistor_SMD:R_0603_1608Metric -> Capacitor_SMD:C_0603_1608Metric; symbol Device:R -> Device:C
- C129: renamed from R154; value 100R 1% (CS filter, Kelvin from the shunt's top) -> 1n; footprint Resistor_SMD:R_0603_1608Metric -> Capacitor_SMD:C_0603_1608Metric; symbol Device:R -> Device:C
- C130: renamed from R156; value 100R 1% (CS filter, Kelvin from the shunt's top) -> 1n; footprint Resistor_SMD:R_0603_1608Metric -> Capacitor_SMD:C_0603_1608Metric; symbol Device:R -> Device:C
- C131: renamed from R158; value 100R 1% (CS filter, Kelvin from the shunt's top) -> 1n; footprint Resistor_SMD:R_0603_1608Metric -> Capacitor_SMD:C_0603_1608Metric; symbol Device:R -> Device:C
- J_DOCK: value spring pins to the dock block (2x6, Preci-Dip 813-S1-012-10-016101, underside): 1-7 GND, 8 SHORE_INHIBIT, 9-10 USB of E6's sensor controller, 11 GND, 12 spare (VIN_RAW crosses on J_VR1-4 since EQ-16) -> spring pins to the dock block (2x6, Preci-Dip 813-S1-012-10-016101, underside): 1-7 GND, 8 SHORE_INHIBIT, 9-10 USB of E6's sensor controller, 11 GND, 12 HOT-R1 hot stop line from E's open drain, pulled up by R216 (SC-50; VIN_RAW crosses on J_VR1-4 since EQ-16)
- R147: renamed from C121; value 10n -> 10R; footprint Capacitor_SMD:C_0603_1608Metric -> Resistor_SMD:R_0603_1608Metric; symbol Device:C -> Device:R
- R149: renamed from C122; value 100n -> 10R; footprint Capacitor_SMD:C_0603_1608Metric -> Resistor_SMD:R_0603_1608Metric; symbol Device:C -> Device:R
- renumbered R147 to R146, R149 to R148
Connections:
- net +3V3: now also R216.2
- net CELL_FUSED: now also R148.1; no longer C121.1
- net CH_ACN: now also R146.1; no longer C128.1
- net CH_ACN_F: now also C121.2, R146.2; no longer C128.2, R147.2
- net CH_ACP_F: now also C121.1, R147.2; no longer R146.2, R147.1
- net CH_SRN_F: now also C122.2, R148.2; no longer C121.2, R149.2
- net CH_SRP_F: now also C122.1, R149.2; no longer R148.2, R149.1
- net DOCK_SPARE: now also R216.1
- net FE_CSF: now also C123.1
- net FE_CSGF: now also C123.2
- net FE_ISNS_N: now also C128.2
- net FE_ISNS_P: now also C128.1, R160.2; no longer C123.2
- net FE_OUT: now also R160.1; no longer C123.1
- net HF_CS: now also R154.1; no longer C129.1
- net HF_CSF: now also C125.1, R154.2; no longer C129.2
- net HF_CSGF: now also C125.2
- net HF_ISNS_N: now also C130.2
- net HF_ISNS_P: now also C130.1, R164.2; no longer C125.2
- net HF_OUT: now also R164.1; no longer C125.1
- net PA_CS: now also R152.1; no longer C122.1
- net PA_CSF: now also C124.1, R152.2; no longer C122.2
- net PA_CSGF: now also C124.2
- net PA_ISNS_N: now also C129.2
- net PA_ISNS_P: now also C129.1, R162.2; no longer C124.2
- net PA_OUT: now also R162.1; no longer C124.1
- net PD_CS: now also R158.1; no longer C131.1
- net PD_CSF: now also C127.1, R158.2; no longer C131.2
- net PD_CSGF: now also C127.2
- net PD_ISNS_P: now also R168.2; no longer C127.2
- net PD_OUT: now also R168.1; no longer C127.1
- net POE_CS: now also R156.1; no longer C130.1
- net POE_CSF: now also C126.1, R156.2; no longer C130.2
- net POE_CSGF: now also C126.2
- net POE_ISNS_N: now also C131.2
- net POE_ISNS_P: now also C131.1, R166.2; no longer C126.2
- net POE_OUT: now also R166.1; no longer C126.1
- net VBAT: now also R149.1; no longer R148.1
- net VBUS20: now also R147.1; no longer R146.1
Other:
- moved on the sheet: R146, R148

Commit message: feat(intent): boards A and B regenerated on the KiCad box from fff04e64 with S-98's interim alignment: the netlists and schematics at parity apart from their dates, the intents carrying the aligned +5V_S2 and +5V_DEV declarations; check_contracts PASS of 99 and the five A to B leads AGREE on the regenerated intents [MESHSAT-1357]
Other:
- note added: "page 1 of 16 MeshSat field kit V2, CERN-OHL-S-2.0 PROTOTYPE, nothing built 2026-09-28"
- note added: "page 10 of 16 MeshSat field kit V2, CERN-OHL-S-2.0 PROTOTYPE, nothing built 2026-09-28"
- note added: "page 11 of 16 MeshSat field kit V2, CERN-OHL-S-2.0 PROTOTYPE, nothing built 2026-09-28"
- note added: "page 12 of 16 MeshSat field kit V2, CERN-OHL-S-2.0 PROTOTYPE, nothing built 2026-09-28"
- note added: "page 13 of 16 MeshSat field kit V2, CERN-OHL-S-2.0 PROTOTYPE, nothing built 2026-09-28"
- note added: "page 14 of 16 MeshSat field kit V2, CERN-OHL-S-2.0 PROTOTYPE, nothing built 2026-09-28"
- note added: "page 15 of 16 MeshSat field kit V2, CERN-OHL-S-2.0 PROTOTYPE, nothing built 2026-09-28"
- note added: "page 16 of 16 MeshSat field kit V2, CERN-OHL-S-2.0 PROTOTYPE, nothing built 2026-09-28"
- note added: "page 2 of 16 MeshSat field kit V2, CERN-OHL-S-2.0 PROTOTYPE, nothing built 2026-09-28"
- note added: "page 3 of 16 MeshSat field kit V2, CERN-OHL-S-2.0 PROTOTYPE, nothing built 2026-09-28"
- note added: "page 4 of 16 MeshSat field kit V2, CERN-OHL-S-2.0 PROTOTYPE, nothing built 2026-09-28"
- note added: "page 5 of 16 MeshSat field kit V2, CERN-OHL-S-2.0 PROTOTYPE, nothing built 2026-09-28"
- note added: "page 6 of 16 MeshSat field kit V2, CERN-OHL-S-2.0 PROTOTYPE, nothing built 2026-09-28"
- note added: "page 7 of 16 MeshSat field kit V2, CERN-OHL-S-2.0 PROTOTYPE, nothing built 2026-09-28"
- note added: "page 8 of 16 MeshSat field kit V2, CERN-OHL-S-2.0 PROTOTYPE, nothing built 2026-09-28"
- note added: "page 9 of 16 MeshSat field kit V2, CERN-OHL-S-2.0 PROTOTYPE, nothing built 2026-09-28"
- note removed: "page 1 of 16 MeshSat field kit V2, CERN-OHL-S-2.0 PROTOTYPE, nothing built 2026-09-27"
- note removed: "page 10 of 16 MeshSat field kit V2, CERN-OHL-S-2.0 PROTOTYPE, nothing built 2026-09-27"
- note removed: "page 11 of 16 MeshSat field kit V2, CERN-OHL-S-2.0 PROTOTYPE, nothing built 2026-09-27"
- note removed: "page 12 of 16 MeshSat field kit V2, CERN-OHL-S-2.0 PROTOTYPE, nothing built 2026-09-27"
- note removed: "page 13 of 16 MeshSat field kit V2, CERN-OHL-S-2.0 PROTOTYPE, nothing built 2026-09-27"
- note removed: "page 14 of 16 MeshSat field kit V2, CERN-OHL-S-2.0 PROTOTYPE, nothing built 2026-09-27"
- note removed: "page 15 of 16 MeshSat field kit V2, CERN-OHL-S-2.0 PROTOTYPE, nothing built 2026-09-27"
- note removed: "page 16 of 16 MeshSat field kit V2, CERN-OHL-S-2.0 PROTOTYPE, nothing built 2026-09-27"
- note removed: "page 2 of 16 MeshSat field kit V2, CERN-OHL-S-2.0 PROTOTYPE, nothing built 2026-09-27"
- note removed: "page 3 of 16 MeshSat field kit V2, CERN-OHL-S-2.0 PROTOTYPE, nothing built 2026-09-27"
- note removed: "page 4 of 16 MeshSat field kit V2, CERN-OHL-S-2.0 PROTOTYPE, nothing built 2026-09-27"
- note removed: "page 5 of 16 MeshSat field kit V2, CERN-OHL-S-2.0 PROTOTYPE, nothing built 2026-09-27"
- note removed: "page 6 of 16 MeshSat field kit V2, CERN-OHL-S-2.0 PROTOTYPE, nothing built 2026-09-27"
- note removed: "page 7 of 16 MeshSat field kit V2, CERN-OHL-S-2.0 PROTOTYPE, nothing built 2026-09-27"
- note removed: "page 8 of 16 MeshSat field kit V2, CERN-OHL-S-2.0 PROTOTYPE, nothing built 2026-09-27"
- note removed: "page 9 of 16 MeshSat field kit V2, CERN-OHL-S-2.0 PROTOTYPE, nothing built 2026-09-27"
